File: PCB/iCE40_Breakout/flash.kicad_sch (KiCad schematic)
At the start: 3 parts, among them U2 W25Q128JVS

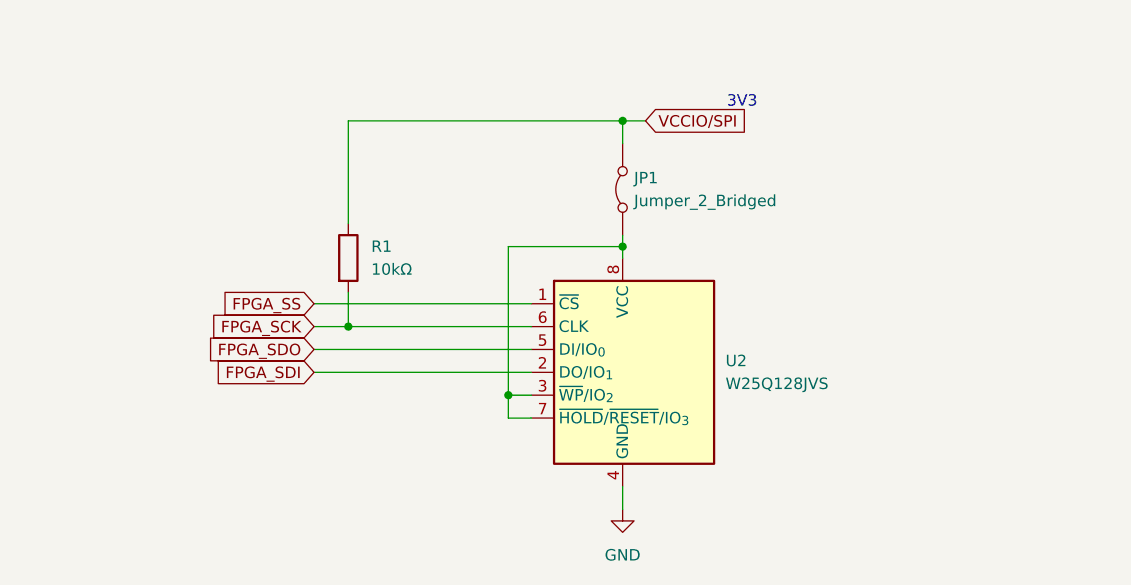
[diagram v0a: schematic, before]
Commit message: Added external programming header
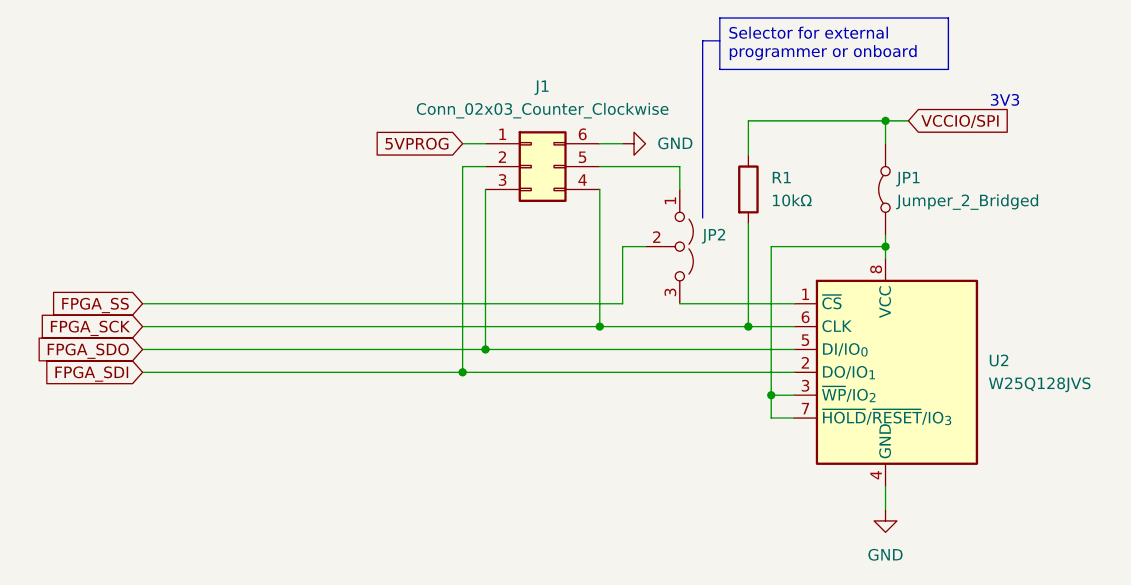
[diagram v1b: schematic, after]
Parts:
- added J1: Conn_02x03_Counter_Clockwise, symbol Connector_Generic:Conn_02x03_Counter_Clockwise
- added JP2: Jumper_3_Open, symbol Jumper:Jumper_3_Open
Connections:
- net FPGA_SCK: now also J1.4 (Pin_4)
- net FPGA_SDI: now also J1.2 (Pin_2)
- net FPGA_SDO: now also J1.3 (Pin_3)
- net FPGA_SS: now also JP2.2 (C); no longer U2.1 (~{CS})
- net GND: now also J1.6 (Pin_6)
- new net: JP2.3 (B), U2.1 (~{CS})
- new net: J1.5 (Pin_5), JP2.1 (A)
- new net 5VPROG: J1.1 (Pin_1)
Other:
- moved on the sheet: JP1, R1, U2

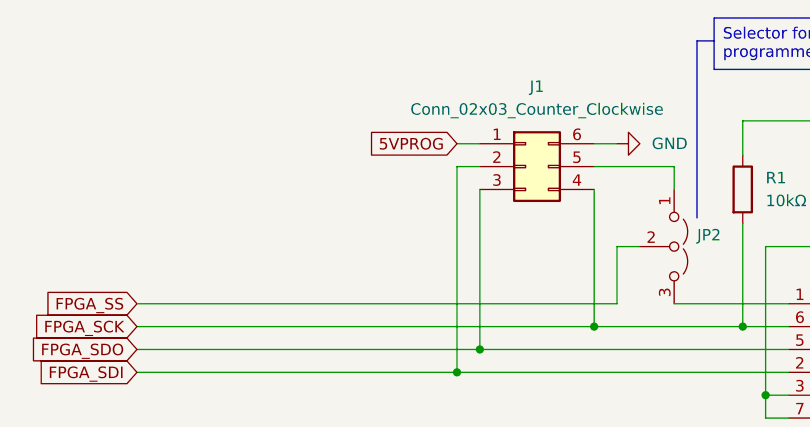
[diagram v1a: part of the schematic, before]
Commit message: Added protection diodes to input power supply
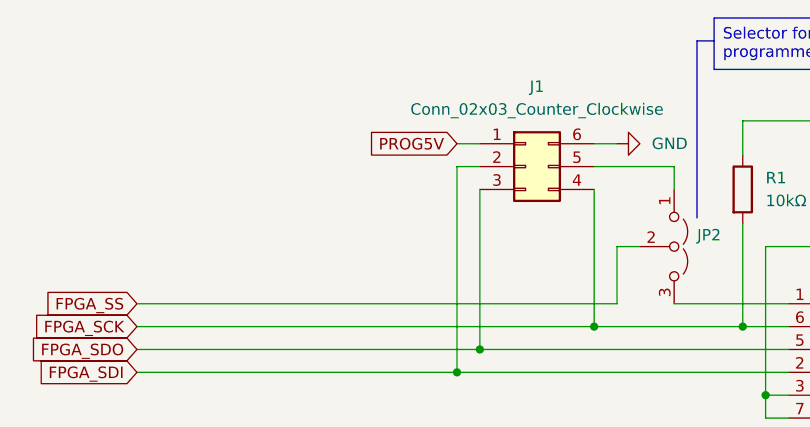
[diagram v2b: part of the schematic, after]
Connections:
- net 5VPROG renamed PROG5V
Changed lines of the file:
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@@
 		)
 	)
-	(global_label "5VPROG"
+	(global_label "PROG5V"
 		(shape input)
 		(at 71.12 36.83 180)

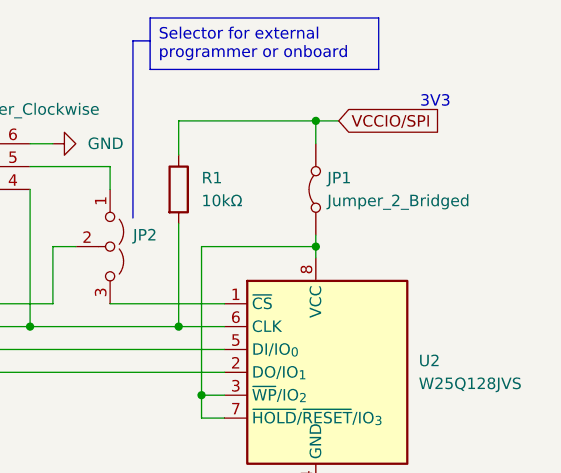
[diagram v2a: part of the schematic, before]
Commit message: Added footprints to all parts, and JLCPCB part numbers
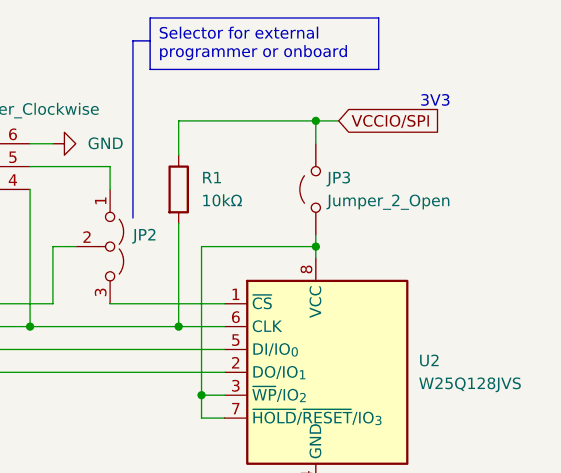
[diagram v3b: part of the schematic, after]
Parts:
- removed JP1: Jumper_2_Bridged, TestPoint:TestPoint_2Pads_Pitch2.54mm_Drill0.8mm, symbol Jumper:Jumper_2_Bridged
- added JP3: Jumper_2_Open, Connector_PinSocket_2.54mm:PinSocket_1x02_P2.54mm_Vertical, symbol Jumper:Jumper_2_Open
- J1: footprint (none) -> Connector_PinSocket_2.54mm:PinSocket_2x03_P2.54mm_Vertical
- JP2: footprint (none) -> Connector_PinSocket_2.54mm:PinSocket_1x03_P2.54mm_Vertical
- R1: footprint (none) -> Resistor_SMD:R_0603_1608Metric; LCSC (none) -> C25804
- U2: LCSC (none) -> C2613930
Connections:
- net VCCIO/SPI: now also JP3.2 (B)
- net at U2.3 (~{WP}/IO_{2}), U2.7 (~{HOLD}/~{RESET}/IO_{3}), U2.8 (VCC): now also JP3.1 (A)
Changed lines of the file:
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@@
+			)
+		)
+		(property "LCSC" "C2613930"
+			(at 118.11 62.23 0)
+			(effects
+				(font
+					(size 1.27 1.27)
+				)
+				(hide yes)
 			)
 		)
@@
 			)
 		)
-		(property "Footprint" ""
+		(property "Footprint" "Connector_PinSocket_2.54mm:PinSocket_1x03_P2.54mm_Vertical"
 			(at 95.25 48.26 0)
 			(effects
@@
 			)
 		)
-		(property "Footprint" ""
+		(property "Footprint" "Resistor_SMD:R_0603_1608Metric"
 			(at 101.092 41.91 90)
 			(effects
@@
 			)
 		)
+		(property "LCSC" "C25804"
+			(at 102.87 41.91 0)
+			(effects
+				(font
+					(size 1.27 1.27)
+				)
+				(hide yes)
+			)
+		)
 		(pin "1"
 		)
@@
 	)
 	(symbol
-		(lib_id "Jumper:Jumper_2_Bridged")
+		(lib_id "Jumper:Jumper_2_Open")
 		(at 118.11 41.91 90)
 		(unit 1)
@@
 		(dnp no)
 		(fields_autoplaced yes)
-		(property "Reference" "JP1"
+		(property "Reference" "JP3"
 			(at 119.38 40.6399 90)
 			(effects
@@
 			)
 		)
-		(property "Value" "Jumper_2_Bridged"
+		(property "Value" "Jumper_2_Open"
 			(at 119.38 43.1799 90)
 			(effects
@@
 			)
 		)
-		(property "Footprint" "TestPoint:TestPoint_2Pads_Pitch2.54mm_Drill0.8mm"
+		(property "Footprint" "Connector_PinSocket_2.54mm:PinSocket_1x02_P2.54mm_Vertical"
 			(at 118.11 41.91 0)
 			(effects
@@
 			)
 		)
-		(property "Description" "Jumper, 2-pole, closed/bridged"
+		(property "Description" "Jumper, 2-pole, open"
 			(at 118.11 41.91 0)
 			(effects
@@
 			)
 		)
+		(pin "1"
+		)
 		(pin "2"
 		)
-		(pin "1"
-		)
-		(instances
-			(project ""
-				(path "/ce4d7974-ef38-4eea-8119-381c4298ef02/0b13b405-f1f0-4313-93f2-3939760c2f72"
-					(reference "JP1")
+		(instances
+			(project "iCE40_Breakout"
+				(path "/ce4d7974-ef38-4eea-8119-381c4298ef02/0b13b405-f1f0-4313-93f2-3939760c2f72"
+					(reference "JP3")
 					(unit 1)
 				)
@@
 			)
 		)
-		(property "Footprint" ""
+		(property "Footprint" "Connector_PinSocket_2.54mm:PinSocket_2x03_P2.54mm_Vertical"
 			(at 78.74 39.37 0)
 			(effects

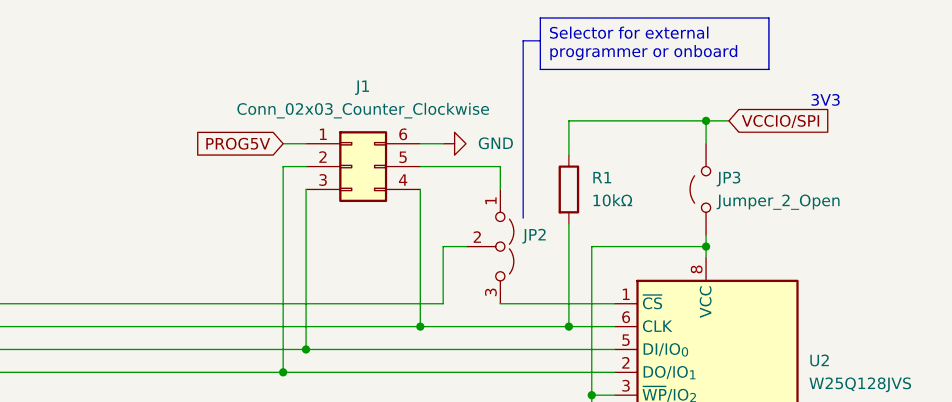
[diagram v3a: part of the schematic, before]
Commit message: Added CDONE and CRESET to programming header
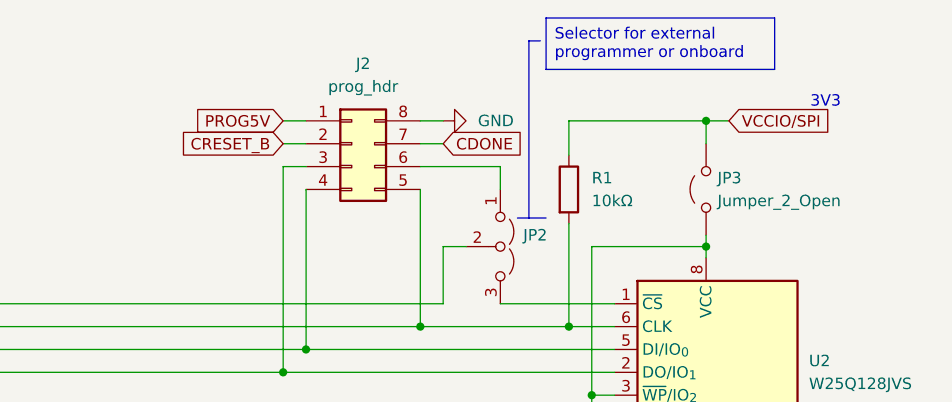
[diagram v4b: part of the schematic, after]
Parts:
- removed J1: Conn_02x03_Counter_Clockwise, Connector_PinSocket_2.54mm:PinSocket_2x03_P2.54mm_Vertical, symbol Connector_Generic:Conn_02x03_Counter_Clockwise
- added J2: prog_hdr, symbol Connector_Generic:Conn_02x04_Counter_Clockwise
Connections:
- net FPGA_SCK: now also J2.5 (Pin_5)
- net FPGA_SDI: now also J2.3 (Pin_3)
- net FPGA_SDO: now also J2.4 (Pin_4)
- net GND: now also J2.8 (Pin_8)
- net PROG5V: now also J2.1 (Pin_1)
- net at JP2.1 (A): now also J2.6 (Pin_6)
- new net CDONE: J2.7 (Pin_7)
- new net CRESET_B: J2.2 (Pin_2)
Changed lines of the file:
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@@
 	(text_box "Selector for external programmer or onboard"
 		(exclude_from_sim no)
-		(at 99.695 22.86 0)
+		(at 100.33 22.86 0)
 		(size 25.4 5.715)
 		(margins 0.9525 0.9525 0.9525 0.9525)
@@
 	(polyline
 		(pts
-			(xy 97.79 25.4) (xy 99.695 25.4)
+			(xy 98.425 25.4) (xy 99.695 25.4)
 		)
 		(stroke
@@
 	(wire
 		(pts
+			(xy 71.12 34.29) (xy 73.66 34.29)
+		)
+		(stroke
+			(width 0)
+			(type default)
+		)
+	)
+	(wire
+		(pts
+			(xy 102.87 57.15) (xy 107.95 57.15)
+		)
+		(stroke
+			(width 0)
+			(type default)
+		)
+	)
+	(polyline
+		(pts
+			(xy 98.425 45.085) (xy 98.425 25.4)
+		)
+		(stroke
+			(width 0)
+			(type default)
+		)
+	)
+	(wire
+		(pts
+			(xy 118.11 74.93) (xy 118.11 77.47)
+		)
+		(stroke
+			(width 0)
+			(type default)
+		)
+	)
+	(wire
+		(pts
+			(xy 102.87 45.72) (xy 102.87 57.15)
+		)
+		(stroke
+			(width 0)
+			(type default)
+		)
+	)
+	(wire
+		(pts
 			(xy 71.12 36.83) (xy 73.66 36.83)
 		)
@@
 	(wire
 		(pts
-			(xy 102.87 57.15) (xy 107.95 57.15)
+			(xy 35.56 54.61) (xy 88.9 54.61)
+		)
+		(stroke
+			(width 0)
+			(type default)
+		)
+	)
+	(wire
+		(pts
+			(xy 86.36 36.83) (xy 88.9 36.83)
+		)
+		(stroke
+			(width 0)
+			(type default)
+		)
+	)
+	(wire
+		(pts
+			(xy 71.12 62.23) (xy 107.95 62.23)
+		)
+		(stroke
+			(width 0)
+			(type default)
+		)
+	)
+	(wire
+		(pts
+			(xy 73.66 39.37) (xy 71.12 39.37)
+		)
+		(stroke
+			(width 0)
+			(type default)
+		)
+	)
+	(wire
+		(pts
+			(xy 118.11 48.26) (xy 118.11 49.53)
 		)
 		(stroke
@@
 	(polyline
 		(pts
-			(xy 97.79 45.085) (xy 97.79 25.4)
-		)
-		(stroke
-			(width 0)
-			(type default)
-		)
-	)
-	(wire
-		(pts
-			(xy 118.11 74.93) (xy 118.11 77.47)
-		)
-		(stroke
-			(width 0)
-			(type default)
-		)
-	)
-	(wire
-		(pts
-			(xy 102.87 45.72) (xy 102.87 57.15)
-		)
-		(stroke
-			(width 0)
-			(type default)
-		)
-	)
-	(wire
-		(pts
-			(xy 35.56 54.61) (xy 88.9 54.61)
-		)
-		(stroke
-			(width 0)
-			(type default)
-		)
-	)
-	(wire
-		(pts
-			(xy 71.12 62.23) (xy 107.95 62.23)
-		)
-		(stroke
-			(width 0)
-			(type default)
-		)
-	)
-	(wire
-		(pts
-			(xy 73.66 39.37) (xy 71.12 39.37)
-		)
-		(stroke
-			(width 0)
-			(type default)
-		)
-	)
-	(wire
-		(pts
-			(xy 118.11 48.26) (xy 118.11 49.53)
+			(xy 97.155 45.085) (xy 98.425 45.085)
 		)
 		(stroke
@@
 	(wire
 		(pts
-			(xy 86.36 36.83) (xy 88.9 36.83)
+			(xy 86.36 34.29) (xy 88.9 34.29)
 		)
 		(stroke
@@
 		(pts
 			(xy 105.41 48.26) (xy 118.11 48.26)
+		)
+		(stroke
+			(width 0)
+			(type default)
+		)
+	)
+	(polyline
+		(pts
+			(xy 98.425 45.085) (xy 100.33 45.085)
 		)
 		(stroke
@@
 	(global_label "PROG5V"
 		(shape input)
-		(at 71.12 36.83 180)
+		(at 71.12 34.29 180)
 		(fields_autoplaced yes)
 		(effects
@@
 		)
 		(property "Intersheetrefs" "${INTERSHEET_REFS}"
-			(at 60.6962 36.83 0)
+			(at 60.6962 34.29 0)
 			(effects
 				(font
@@
 				)
 				(justify right)
+				(hide yes)
+			)
+		)
+	)
+	(global_label "CRESET_B"
+		(shape input)
+		(at 71.12 36.83 180)
+		(fields_autoplaced yes)
+		(effects
+			(font
+				(size 1.27 1.27)
+			)
+			(justify right)
+		)
+		(property "Intersheetrefs" "${INTERSHEET_REFS}"
+			(at 58.8821 36.83 0)
+			(effects
+				(font
+					(size 1.27 1.27)
+				)
+				(justify right)
+				(hide yes)
+			)
+		)
+	)
+	(global_label "CDONE"
+		(shape input)
+		(at 88.9 36.83 0)
+		(fields_autoplaced yes)
+		(effects
+			(font
+				(size 1.27 1.27)
+			)
+			(justify left)
+		)
+		(property "Intersheetrefs" "${INTERSHEET_REFS}"
+			(at 98.2352 36.83 0)
+			(effects
+				(font
+					(size 1.27 1.27)
+				)
+				(justify left)
 				(hide yes)
 			)
@@
 	)
 	(symbol
+		(lib_id "Connector_Generic:Conn_02x04_Counter_Clockwise")
+		(at 78.74 36.83 0)
+		(unit 1)
+		(exclude_from_sim no)
+		(in_bom yes)
+		(on_board yes)
+		(dnp no)
+		(fields_autoplaced yes)
+		(property "Reference" "J2"
+			(at 80.01 27.94 0)
+			(effects
+				(font
+					(size 1.27 1.27)
+				)
+			)
+		)
+		(property "Value" "prog_hdr"
+			(at 80.01 30.48 0)
+			(effects
+				(font
+					(size 1.27 1.27)
+				)
+			)
+		)
+		(property "Footprint" ""
+			(at 78.74 36.83 0)
+			(effects
+				(font
+					(size 1.27 1.27)
+				)
+				(hide yes)
+			)
+		)
+		(property "Datasheet" "~"
+			(at 78.74 36.83 0)
+			(effects
+				(font
+					(size 1.27 1.27)
+				)
+				(hide yes)
+			)
+		)
+		(property "Description" "Generic connector, double row, 02x04, counter clockwise pin numbering scheme (similar to DIP package numbering), script generated (kicad-library-utils/schlib/autogen/connector/)"
+			(at 78.74 36.83 0)
+			(effects
+				(font
+					(size 1.27 1.27)
+				)
+				(hide yes)
+			)
+		)
+		(pin "2"
+		)
+		(pin "4"
+		)
+		(pin "1"
+		)
+		(pin "3"
+		)
+		(pin "6"
+		)
+		(pin "5"
+		)
+		(pin "7"
+		)
+		(pin "8"
+		)
+		(instances
+			(project ""
+				(path "/ce4d7974-ef38-4eea-8119-381c4298ef02/0b13b405-f1f0-4313-93f2-3939760c2f72"
+					(reference "J2")
+					(unit 1)
+				)
+			)
+		)
+	)
+	(symbol
 		(lib_id "Memory_Flash:W25Q128JVS")
 		(at 118.11 62.23 0)
@@
 	(symbol
 		(lib_id "power:GND")
-		(at 88.9 36.83 90)
+		(at 88.9 34.29 90)
 		(unit 1)
 		(exclude_from_sim no)
@@
 		(fields_autoplaced yes)
 		(property "Reference" "#PWR024"
-			(at 95.25 36.83 0)
+			(at 95.25 34.29 0)
 			(effects
 				(font
@@
 		)
 		(property "Value" "GND"
-			(at 92.7567 36.8299 90)
+			(at 92.7567 34.2899 90)
 			(effects
 				(font
@@
 		)
 		(property "Footprint" ""
-			(at 88.9 36.83 0)
+			(at 88.9 34.29 0)
 			(effects
 				(font
@@
 		)
 		(property "Datasheet" ""
-			(at 88.9 36.83 0)
+			(at 88.9 34.29 0)
 			(effects
 				(font
@@
 		)
 		(property "Description" "Power symbol creates a global label with name \"GND\" , ground"
-			(at 88.9 36.83 0)
+			(at 88.9 34.29 0)
 			(effects
 				(font
@@
 					(unit 1)
 				)
-			)
-		)
-	)
-	(symbol
-		(lib_id "Connector_Generic:Conn_02x03_Counter_Clockwise")
-		(at 78.74 39.37 0)
-		(unit 1)
-		(exclude_from_sim no)
-		(in_bom yes)
-		(on_board yes)
-		(dnp no)
-		(fields_autoplaced yes)
-		(property "Reference" "J1"
-			(at 80.01 30.48 0)
-			(effects
-				(font
-					(size 1.27 1.27)
-				)
-			)
-		)
-		(property "Value" "Conn_02x03_Counter_Clockwise"
-			(at 80.01 33.02 0)
-			(effects
-				(font
-					(size 1.27 1.27)
-				)
-			)
-		)
-		(property "Footprint" "Connector_PinSocket_2.54mm:PinSocket_2x03_P2.54mm_Vertical"
-			(at 78.74 39.37 0)
-			(effects
-				(font
-					(size 1.27 1.27)
-				)
-				(hide yes)
-			)
-		)
-		(property "Datasheet" "~"
-			(at 78.74 39.37 0)
-			(effects
-				(font
-					(size 1.27 1.27)
-				)
-				(hide yes)
-			)
-		)
-		(property "Description" "Generic connector, double row, 02x03, counter clockwise pin numbering scheme (similar to DIP package numbering), script generated (kicad-library-utils/schlib/autogen/connector/)"
-			(at 78.74 39.37 0)
-			(effects
-				(font
-					(size 1.27 1.27)
-				)
-				(hide yes)
-			)
-		)
-		(pin "1"
-		)
-		(pin "6"
-		)
-		(pin "2"
-		)
-		(pin "5"
-		)
-		(pin "3"
-		)
-		(pin "4"
-		)
-		(instances
-			(project ""
-				(path "/ce4d7974-ef38-4eea-8119-381c4298ef02/0b13b405-f1f0-4313-93f2-3939760c2f72"
-					(reference "J1")
-					(unit 1)
-				)
